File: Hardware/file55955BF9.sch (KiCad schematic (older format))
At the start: 40 parts

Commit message: es ist wohl ein größerer stm32 nötig. mit mehr pins.
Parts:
- removed Q? (x2): IRF7309IPBF, SO-8, symbol IRF7309IPBF
- added Q201, Q202: CSD18532Q5B, symbol Q_NMOS_SGD
- added R215: 0*, symbol R
- C212: renamed from C?; Digikey-Nummer (none) -> 445-3917-1-ND
- C217: renamed from C?; value 1u -> 22u; Digikey-Nummer (none) -> 490-1882-1-ND
- L202: renamed from L?; Digikey-Nummer (none) -> 732-1352-1-ND
- gave numbers to parts that had none: 35
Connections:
- net labels added: GNDPWR
- wire segments 60 -> 58
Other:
- note removed: "SO8 dual FET - 55V"

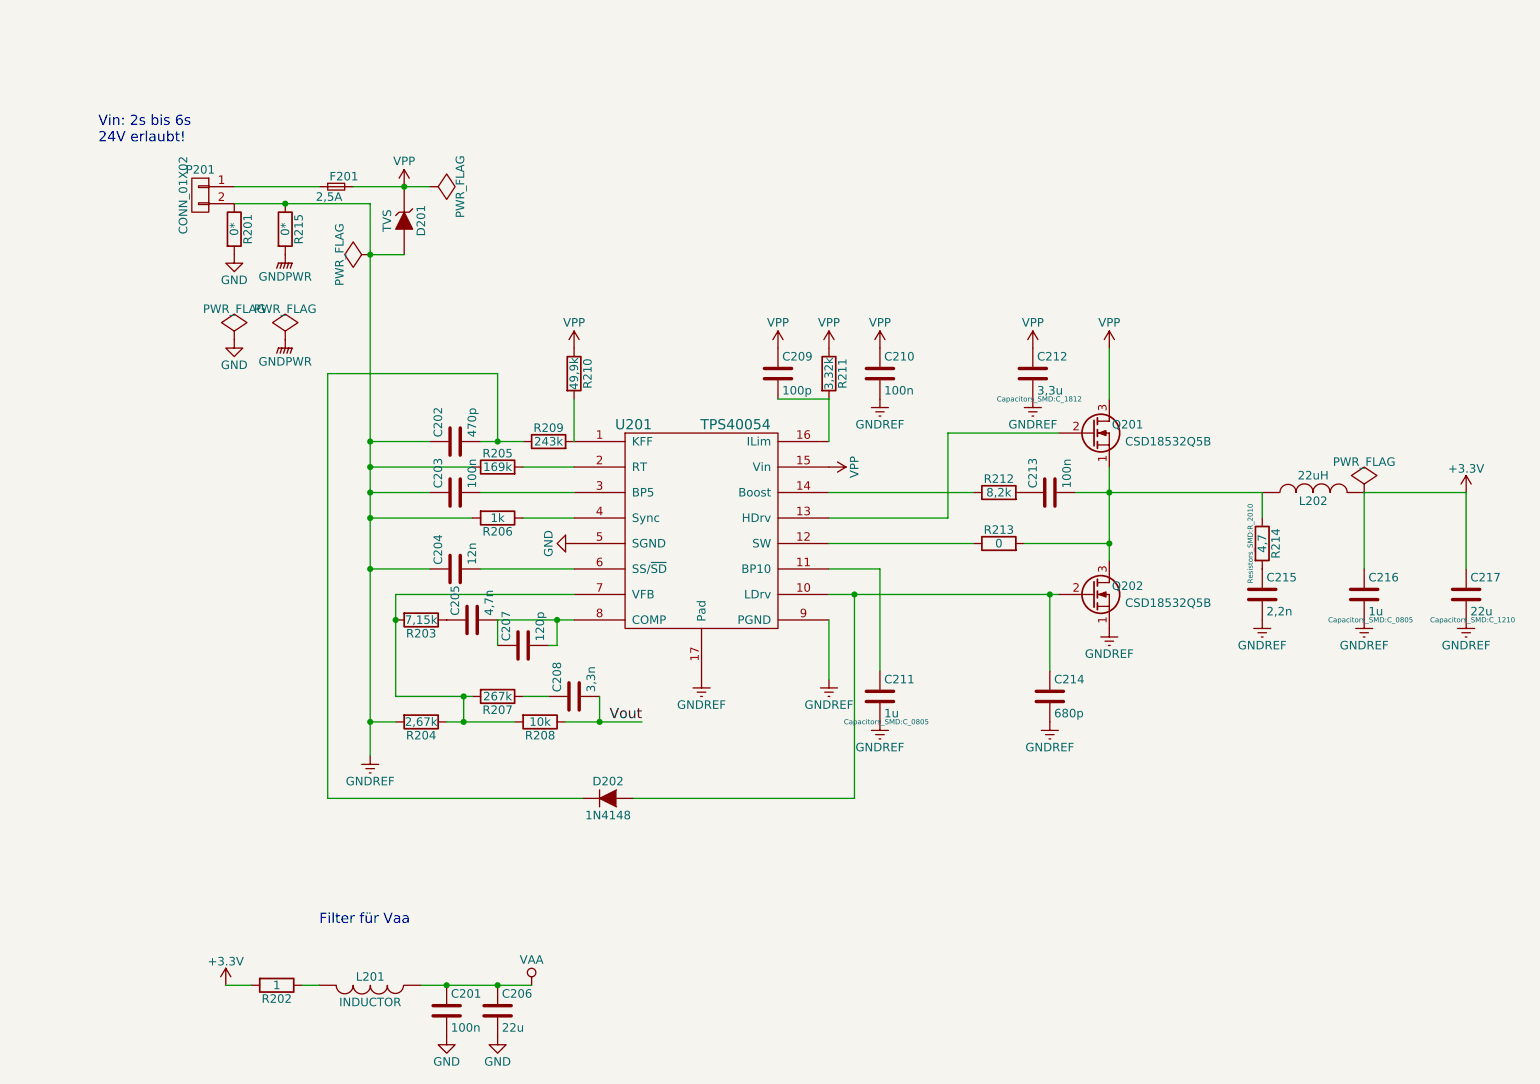
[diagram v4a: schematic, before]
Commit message: Schaltplan momentan fertig - Netzliste angefangen.
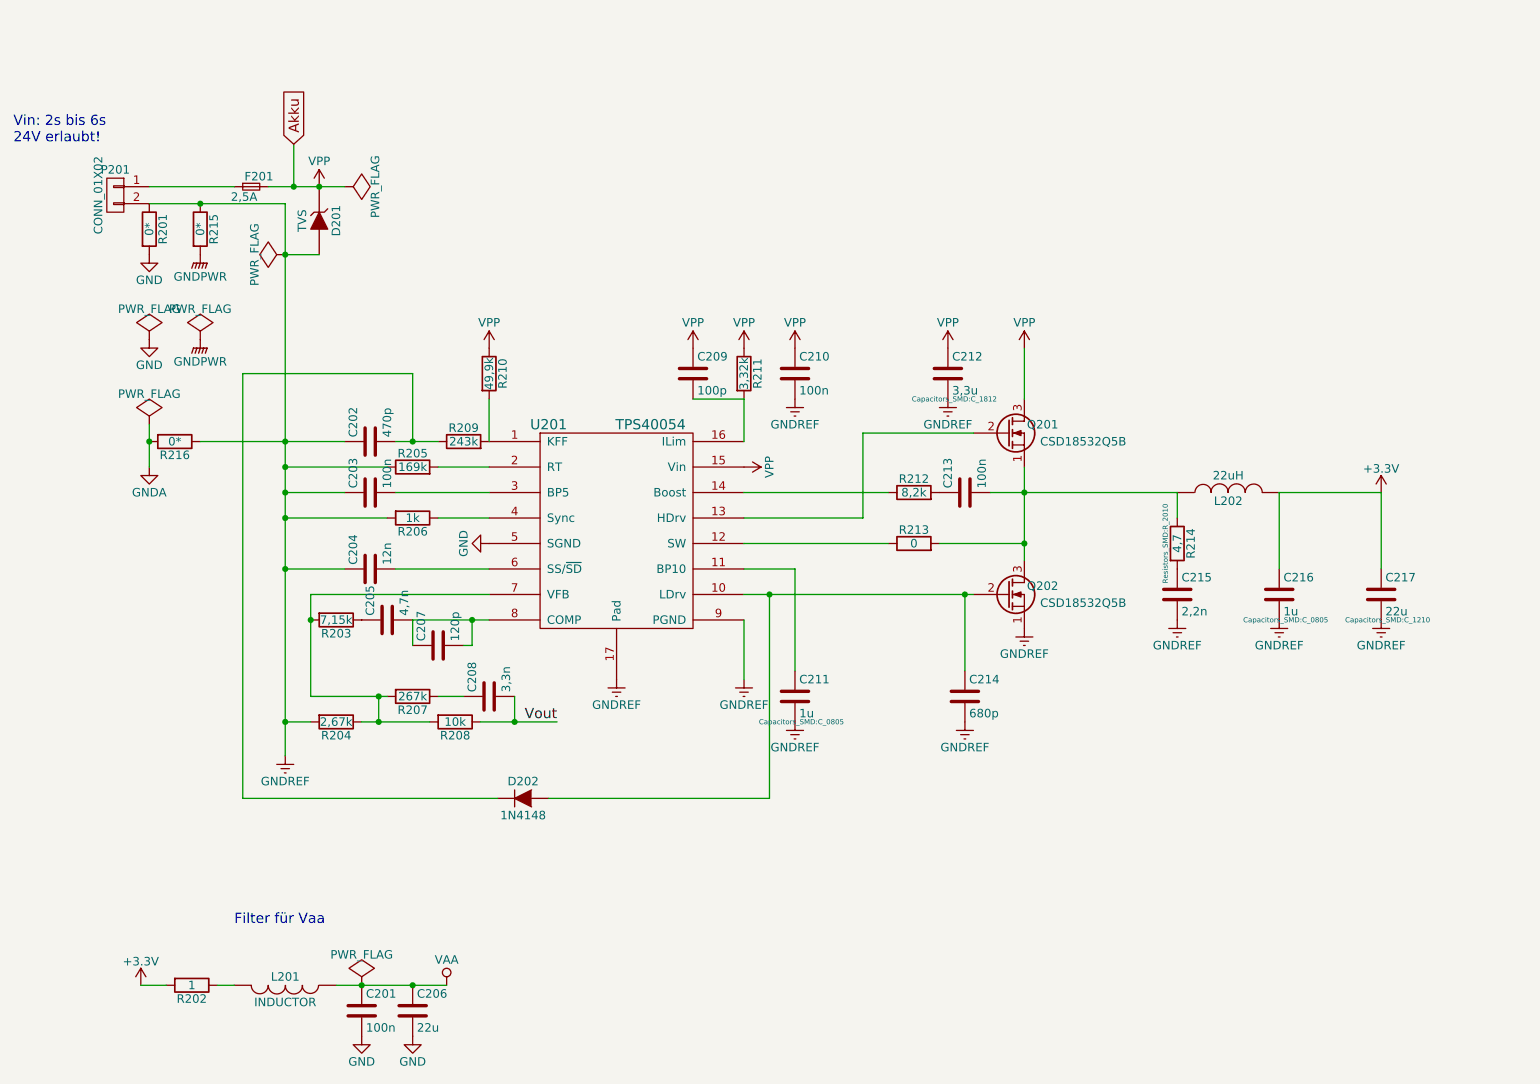
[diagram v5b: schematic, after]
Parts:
- added R216: 0*, Resistors_SMD:R_0603, symbol R
- P201: footprint (none) -> Pin_Headers:Pin_Header_Straight_1x02
- R201, R202, R215: footprint (none) -> Resistors_SMD:R_0603
- U201: footprint (none) -> Housings_SSOP:TSSOP-16-1EP_4.4x5mm_Pitch0.65mm
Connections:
- net GNDREF: now also R216.1
- new net GNDA: R216.2
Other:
- moved on the sheet: C201, C202, C203, C204, C205, C206, C207, C208, C209, C210, C211, C212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

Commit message: Platine angefangen - es wird auf jeden Fall eng
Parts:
- D201: value TVS -> VC120630D650RP; footprint (none) -> Capacitors_SMD:C_1206
- L201: value INDUCTOR -> EMI Filter; footprint (none) -> Resistors_SMD:R_0805
- L202: footprint (none) -> Choke_SMD:Choke_SMD_Wuerth-WE-PD-Typ-LS
- Q201, Q202: footprint (none) -> PhilippsFootprints:SON5x6_FET_123

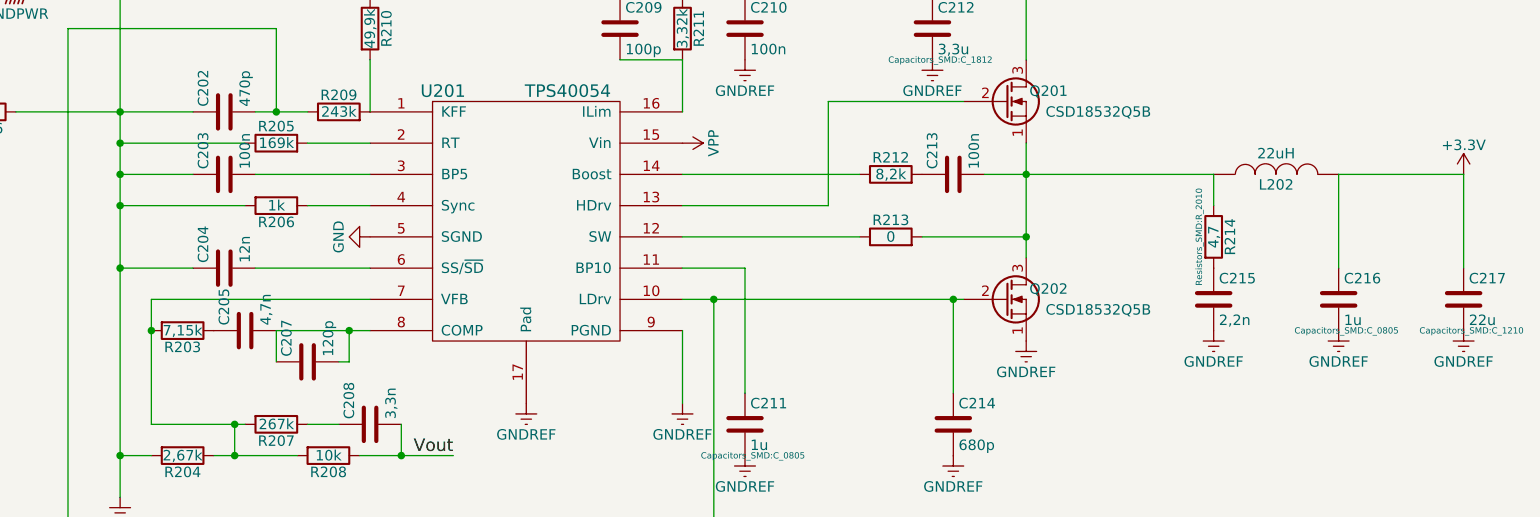
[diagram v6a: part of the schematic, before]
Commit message: Schaltwandler fast fertig
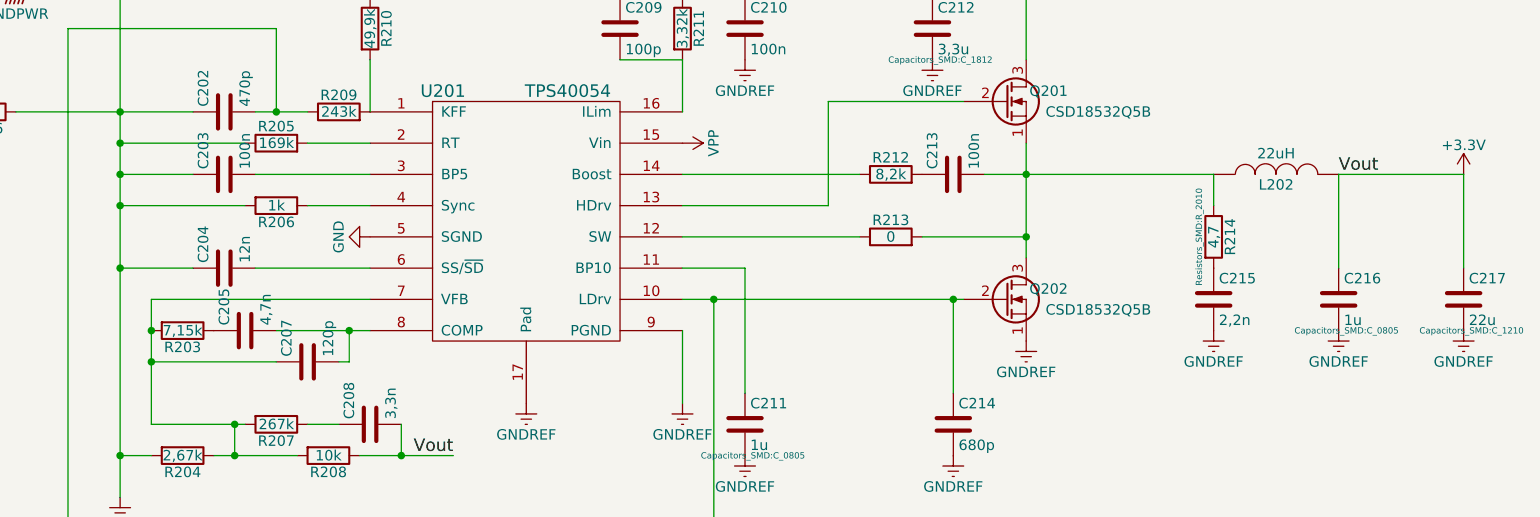
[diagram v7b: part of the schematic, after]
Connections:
- net Vout is gone; now on net +3V3: C208.2, R208.1
- net at R203.2, R204.1, R207.2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: now also C207.1
- net at C205.2, C207.2, U201.8 (COMP): no longer C207.1
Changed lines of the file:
@@
 Connection ~ 4200 4450
-Wire Wire Line
-	3850 4450 3850 4600
 Wire Wire Line
 	3250 4300 3250 4900
@@
 	1    0    0    -1
 $EndComp
+Wire Wire Line
+	3850 4600 3250 4600
+Connection ~ 3250 4600
+Text Label 8950 3700 0    60   ~ 0
+Vout
 $EndSCHEMATC

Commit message: platine fast fertig.
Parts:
- added D? (x2): STPS340U, Diodes_SMD:Diode-SMB_Standard, symbol D_Schottky
- added P?: CONN_01X02, Pin_Headers:Pin_Header_Straight_1x02, symbol CONN_01X02
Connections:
- net GNDREF: now also P?.2 (P2)
- net at P201.1 (P1): now also D?.2 (A); no longer F201.1
- new net: D?.1 (K), D?.1 (K), F201.1
- new net: D?.2 (A), P?.1 (P1)
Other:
- note added: "Anschluss von zwei Akkus sinnvoll, damit bei Ausfall die Schaltung weiter versorgt werden kann."
